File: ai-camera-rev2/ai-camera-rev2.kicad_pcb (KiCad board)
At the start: 4 copper layers, 70 x 70 mm, 176 parts, among them J1 Conn-01x02_P2mm_NONAME_JST-PH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, J2 TYPE-C-31-M-12, J3 DBG, J4 Conn-02x10_P2.54mm_B-2100S20P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, J5 Conn-01x02_P1.25mm_10114829-1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, J6 Conn_01x24_FFC_0.5mm_AFC01-S2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, Q1 2N7002, Q2 2N7002, Q3 AO3401A, Q4 AO3401A, Q5 2N7002, Q6 AO3401A, Q7 2N7002, Q8 AO3401A, Q9 2N7002, SW1 SW_PB_90deg_K2-1102AQ-H4CW-01, SW2 SW_PB_TS-1187A-B-A-B, SW3 SW_PB_TS-1187A-B-A-B, SW4 SW_PB_90deg_K2-1102AQ-H4CW-01, U1 TP4057-42-SOT26-R, U10 ESP32-S3-WROOM-1-N16R8, U11 MT9284-28J, U12 LTR-303ALS-01, U2 XC6206-2.8V, U3 PCF85063AT_SO8, U4 SOT-23-6_SN74LVC1G373DBVR_TI, U5 SY8089AAAC, U6 PIR_AS312, U7 XC6206-2.8V, U8 RT9166-12GVL, U9 AP1511B, Y1 32.768kHz_Q13FC1350000400

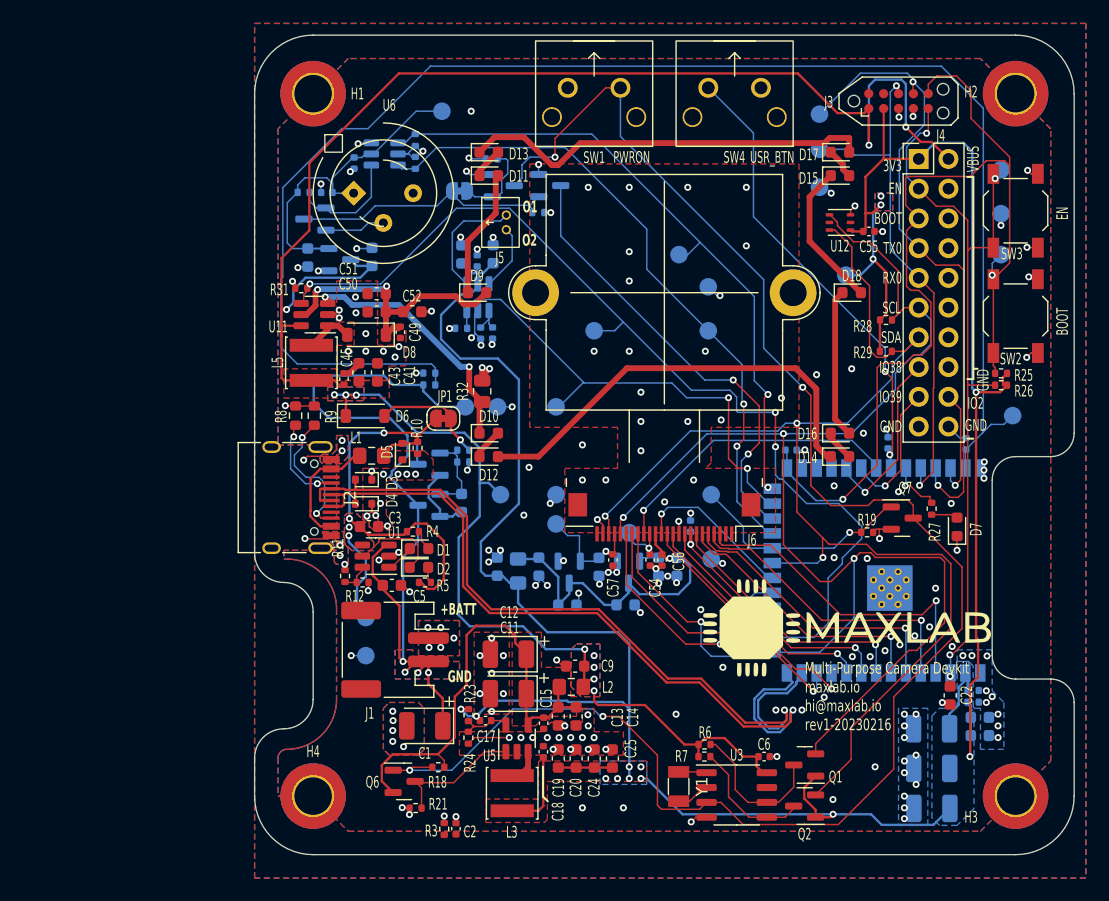
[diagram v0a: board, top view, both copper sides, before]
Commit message: EAC-49: move ALS, PIR and improve power routing
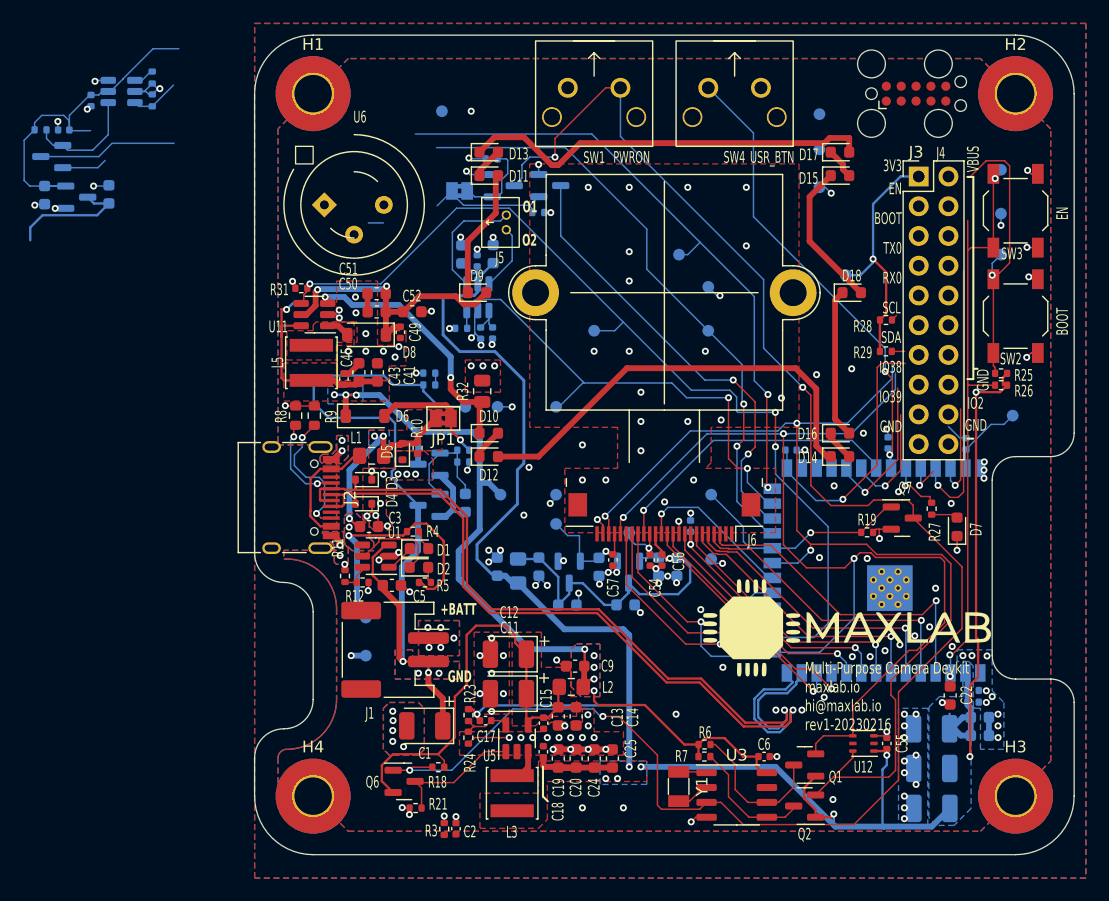
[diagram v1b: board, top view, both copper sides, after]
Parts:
- H1, H2, H3, H4: value M3 -> MountingHole_Pad; footprint MountingHole:MountingHole_3.2mm_M3_DIN965_Pad_TopBottom -> MountingHole:MountingHole_3.2mm_M3_Pad_TopBottom
- J3: value DBG -> MAXLAB; footprint Connector:Tag-Connect_TC2050-IDC-NL_2x05_P1.27mm_Vertical -> Connector:Tag-Connect_TC2050-IDC-FP_2x05_P1.27mm_Vertical
- JP1: value CUT_USB -> USB_PWR; footprint Jumper:SolderJumper-2_P1.3mm_Bridged_RoundedPad1.0x1.5mm -> Jumper:SolderJumper-2_P1.3mm_Bridged2Bar_Pad1.0x1.5mm
- JP2: value CUT_PIR -> SolderJumper_2_Bridged; footprint Jumper:SolderJumper-2_P1.3mm_Bridged_RoundedPad1.0x1.5mm -> Jumper:SolderJumper-2_P1.3mm_Bridged2Bar_Pad1.0x1.5mm
- TP1, TP10, TP11, TP12, TP13, TP14, TP15, TP16, TP17, TP18, TP19, TP2, TP20, TP21, TP22, TP23, TP24, TP3, TP4, TP5, TP6, TP7, TP8, TP9: value TP -> TestPoint; footprint TestPoint:TestPoint_Pad_D1.5mm -> TestPoint:TestPoint_Pad_D1.0mm
- moved U12 44.5 mm to (147.0, 105.5)
- moved C55 43.8 mm to (149.0, 105.5), turned to 90 degrees
- moved C7 23.1 mm to (77.1, 58.7)
- moved Q8 23.1 mm to (77.7, 55.4)
- moved R15 23.1 mm to (86.3, 50.6)
- moved R16 23.1 mm to (86.3, 48.6)
- moved C10 23.1 mm to (81.0, 50.6)
- moved C16 23.1 mm to (78.7, 53.1)
- moved C4 23.1 mm to (82.6, 58.6)
- moved R20 23.1 mm to (76.7, 53.1)
- moved U2 23.1 mm to (79.8, 58.8)
- moved U4 23.1 mm to (83.6, 49.8)
- moved U6 2.69 mm to (103.5, 59.5)
- moved J3 1.63 mm to (151.5, 50.0)
- moved J4 1.50 mm to (151.7, 57.1)
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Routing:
- net /BATT_DETECT: track 129.1 -> 7.68 mm
- net VBUS: track 185.0 -> 112.5 mm, vias 11 -> 9
- net /RXD0: track 44.9 -> 3.18 mm, vias 2 -> 1
- net /ESP_BOOT: track 84.8 -> 46.8 mm
- net /TXD0: track 55.0 -> 23.3 mm, vias 2 -> 1
- net +3V3: track 231.3 -> 202.4 mm, vias 14 -> 10
- net /CAM.SCL: track 113.9 -> 92.7 mm
- net /ESP_EN: track 65.6 -> 52.0 mm, vias 4 -> 3
- net /CAM.SDA: track 105.9 -> 92.3 mm
- net Net-(D6-A): track 9.65 -> 15.6 mm
- net /IRLED_PWM: track 84.0 -> 79.9 mm
- net +BATT: track 68.9 -> 65.7 mm
- net Net-(Q3-G): track 7.14 -> 9.88 mm
- net /IO38: track 14.8 -> 12.3 mm
- net +5V: track 42.3 -> 39.8 mm, vias 4 -> 5
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- added copper zone on F.Cu, net Net-(D8-A)

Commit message: EAC-49: finish with all traces routing
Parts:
- moved R29 38.5 mm to (144.5, 110.2), turned to 90 degrees
- moved R28 37.4 mm to (144.5, 106.5), turned to 90 degrees
- moved Q8 31.4 mm to (109.0, 53.0), turned to 0 degrees
- moved U2 27.3 mm to (107.0, 56.5)
- moved C4 27.3 mm to (109.8, 56.5), turned to 90 degrees
- moved C7 27.3 mm to (104.2, 56.5)
- moved R15 25.8 mm to (112.0, 49.2), turned to 180 degrees
- moved R16 25.7 mm to (112.0, 48.2), turned to 180 degrees
- moved R20 25.6 mm to (102.0, 57.0), turned to 90 degrees
- moved U4 25.4 mm to (109.0, 49.5)
- moved C10 25.0 mm to (106.0, 49.5), turned to 180 degrees
- moved C16 22.6 mm to (101.0, 57.0), turned to 90 degrees
- moved C29 7.80 mm to (113.0, 63.0), turned to 90 degrees
- moved C28 7.46 mm to (114.0, 63.0), turned to 90 degrees
- moved R30 7.43 mm to (115.0, 63.0), turned to -90 degrees
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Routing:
- net VBUS: track 112.5 -> 209.0 mm, vias 9 -> 11
- net /BATT_DETECT: track 7.68 -> 76.7 mm, vias 0 -> 2
- net /RXD0: track 3.18 -> 56.5 mm, vias 1 -> 3
- net /TXD0: track 23.3 -> 50.9 mm, vias 1 -> 3
- net /ESP_BOOT: track 46.8 -> 72.4 mm, vias 2 -> 3
- net /PWR_PIR: track 29.0 -> 48.9 mm
- net Net-(Q8-S): track 5.17 -> 19.0 mm
- net /ESP_EN: track 52.0 -> 65.0 mm
- net +3V3: track 202.4 -> 212.7 mm, vias 10 -> 16
- net Net-(JP2-A): track 22.5 -> 15.0 mm
- net Net-(J5-Pin_1): track 5.65 -> 13.1 mm
- net Net-(J5-Pin_2): track 10.1 -> 17.0 mm
- net /CAM.SCL: track 92.7 -> 99.2 mm
- net /IRCUT_CTRL: track 41.5 -> 45.9 mm
- net GND: track 100.9 -> 103.8 mm, vias 201 -> 209
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
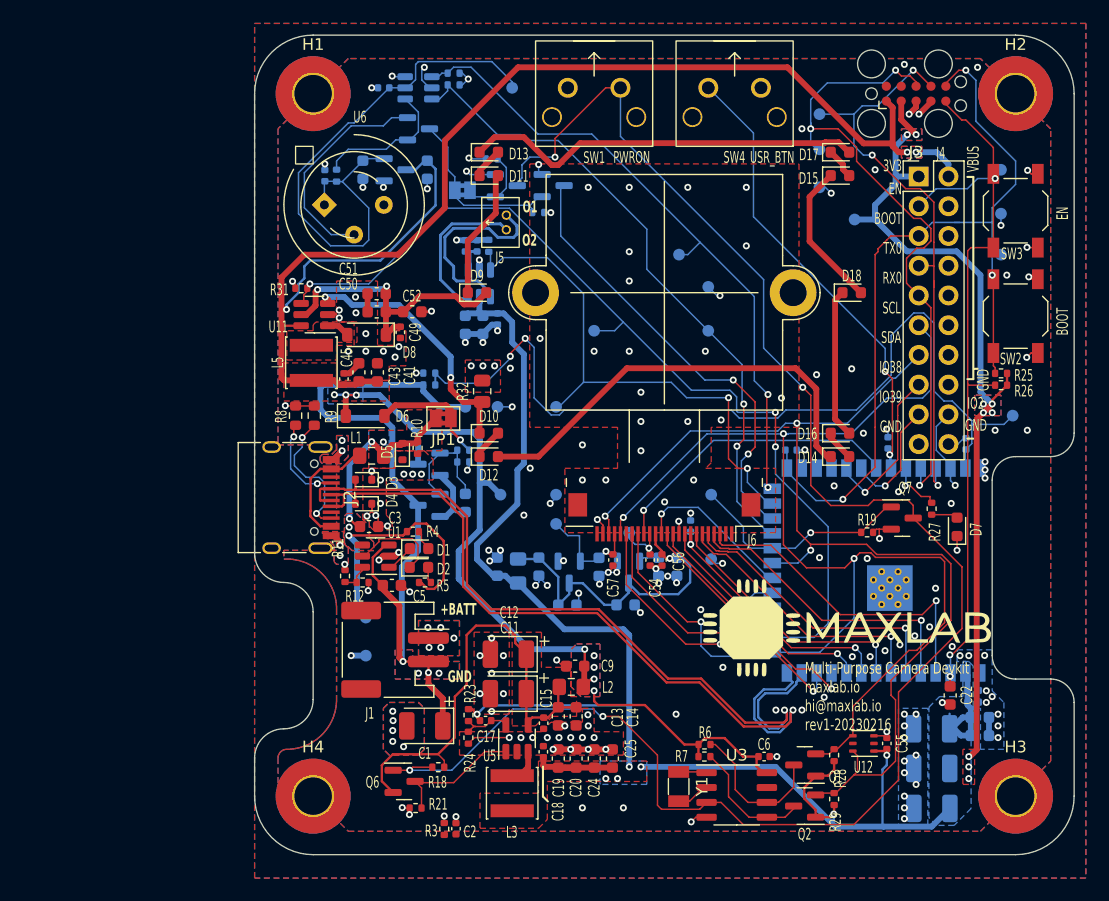
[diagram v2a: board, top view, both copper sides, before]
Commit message: EAC-49: update silkscreen and use single capacitor for all decoupling
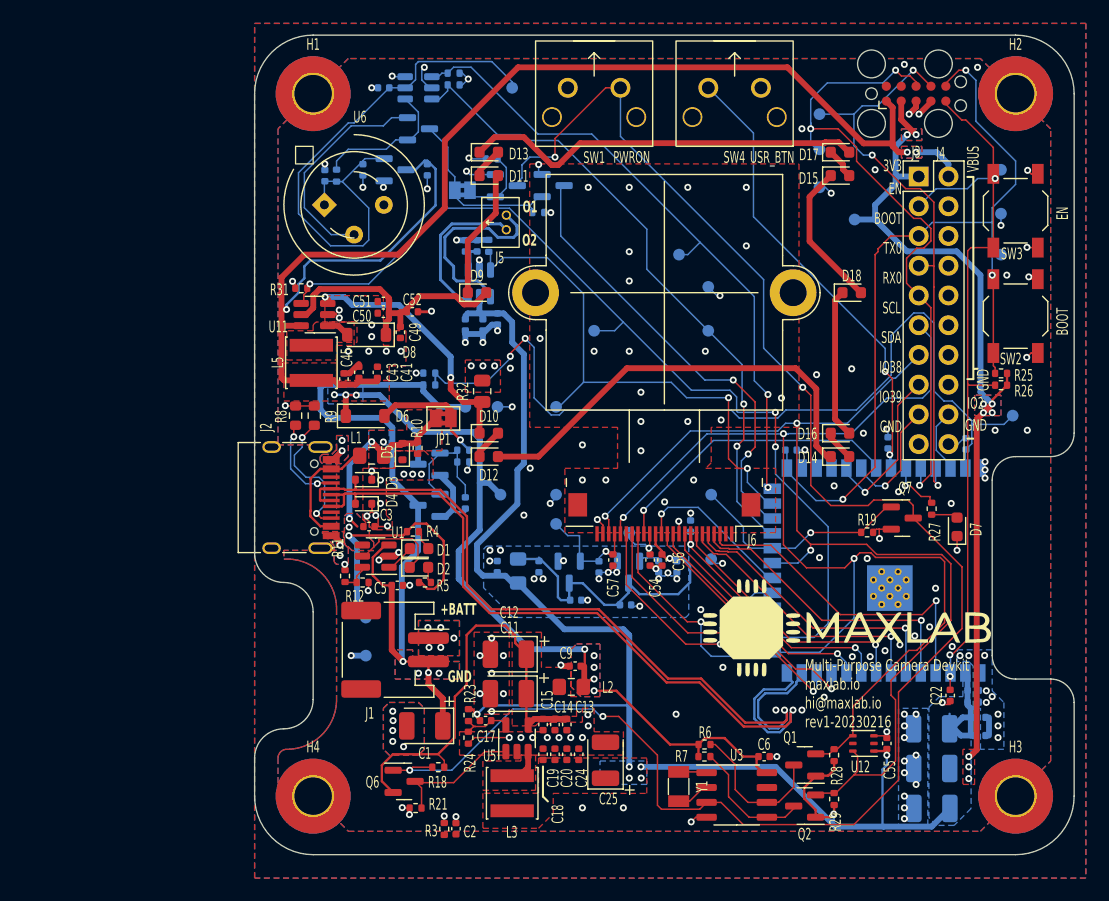
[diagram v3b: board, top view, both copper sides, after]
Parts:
- C10, C15, C16, C18, C2, C21, C23, C28, C29, C32, C33, C45, C46, C47, C49, C54, C55, C56, C57, C6: value 100n_0402_CL05B104KB54PNC -> 10u_0402_CL05A105KA5NQNC
- C13, C19, C20, C22, C24, C26, C27, C30, C31, C34, C35, C36, C37, C4, C41, C42, C5, C53, C7, C8, C9: value 10u_0603_CL10A106KP8NNNC -> 10u_0402_CL05A105KA5NQNC; footprint Capacitor_SMD:C_0603_1608Metric -> Capacitor_SMD:C_0402_1005Metric
- C14, C3, C43, C44, C50, C51, C52: value 1u_0603_CL10A105KB8NNNC -> 10u_0402_CL05A105KA5NQNC; footprint Capacitor_SMD:C_0603_1608Metric -> Capacitor_SMD:C_0402_1005Metric
- C25: value 10u_0603_CL10A106KP8NNNC -> 100u_CASE-B-3528_TAJB107K006RNJ; footprint Capacitor_SMD:C_0603_1608Metric -> 00-kiml-capacitor-tantalum:CP_EIA-3528-15_AVX-H
- moved C24 1.37 mm to (122.7, 106.4)
- moved C13 1.06 mm to (121.7, 103.9)
- moved C51 0.88 mm to (106.0, 67.8)
- moved C20 0.87 mm to (121.7, 106.4)
- moved C30 0.83 mm to (122.4, 93.3)
- moved C14 0.75 mm to (120.7, 103.9)
- moved C25 0.61 mm to (125.0, 106.9), turned to 90 degrees
- moved C50 0.58 mm to (106.0, 68.8)
- moved C5 0.47 mm to (107.2, 92.0)
- moved C19 0.46 mm to (120.7, 106.4)
- moved C18 0.21 mm to (119.6, 106.4)
- moved C15 0.13 mm to (119.6, 103.9)
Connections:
- C25 pad 1: GND -> +3V3
- C25 pad 2: +3V3 -> GND
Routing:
- net GND: track 103.8 -> 89.5 mm, vias 209 -> 201
- net +3V3: track 212.7 -> 200.0 mm
- net Net-(Q6-S): track 39.4 -> 37.0 mm
- net /IO2: track 7.16 -> 5.22 mm, vias 1 -> 0
- net /CAM.SDA: track 91.9 -> 91.0 mm
- net Net-(D8-K): track 24.5 -> 23.7 mm, vias 2 -> 0
- net /ESP_BOOT: track 72.4 -> 71.7 mm
- net Net-(JP2-B): track 6.06 -> 5.36 mm
- net Net-(J5-Pin_2): track 17.0 -> 16.4 mm
- net /PIR_CTRL_LE: track 55.1 -> 54.5 mm
- net VBUS: track 209.0 -> 208.5 mm
- net /TXD0: track 50.9 -> 50.4 mm
- added copper zone on F.Cu, net Net-(U5-LX)
